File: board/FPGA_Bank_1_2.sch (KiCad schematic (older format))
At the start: 3 parts, among them SW1 SW_PUSH, U10 XC6SLX150T

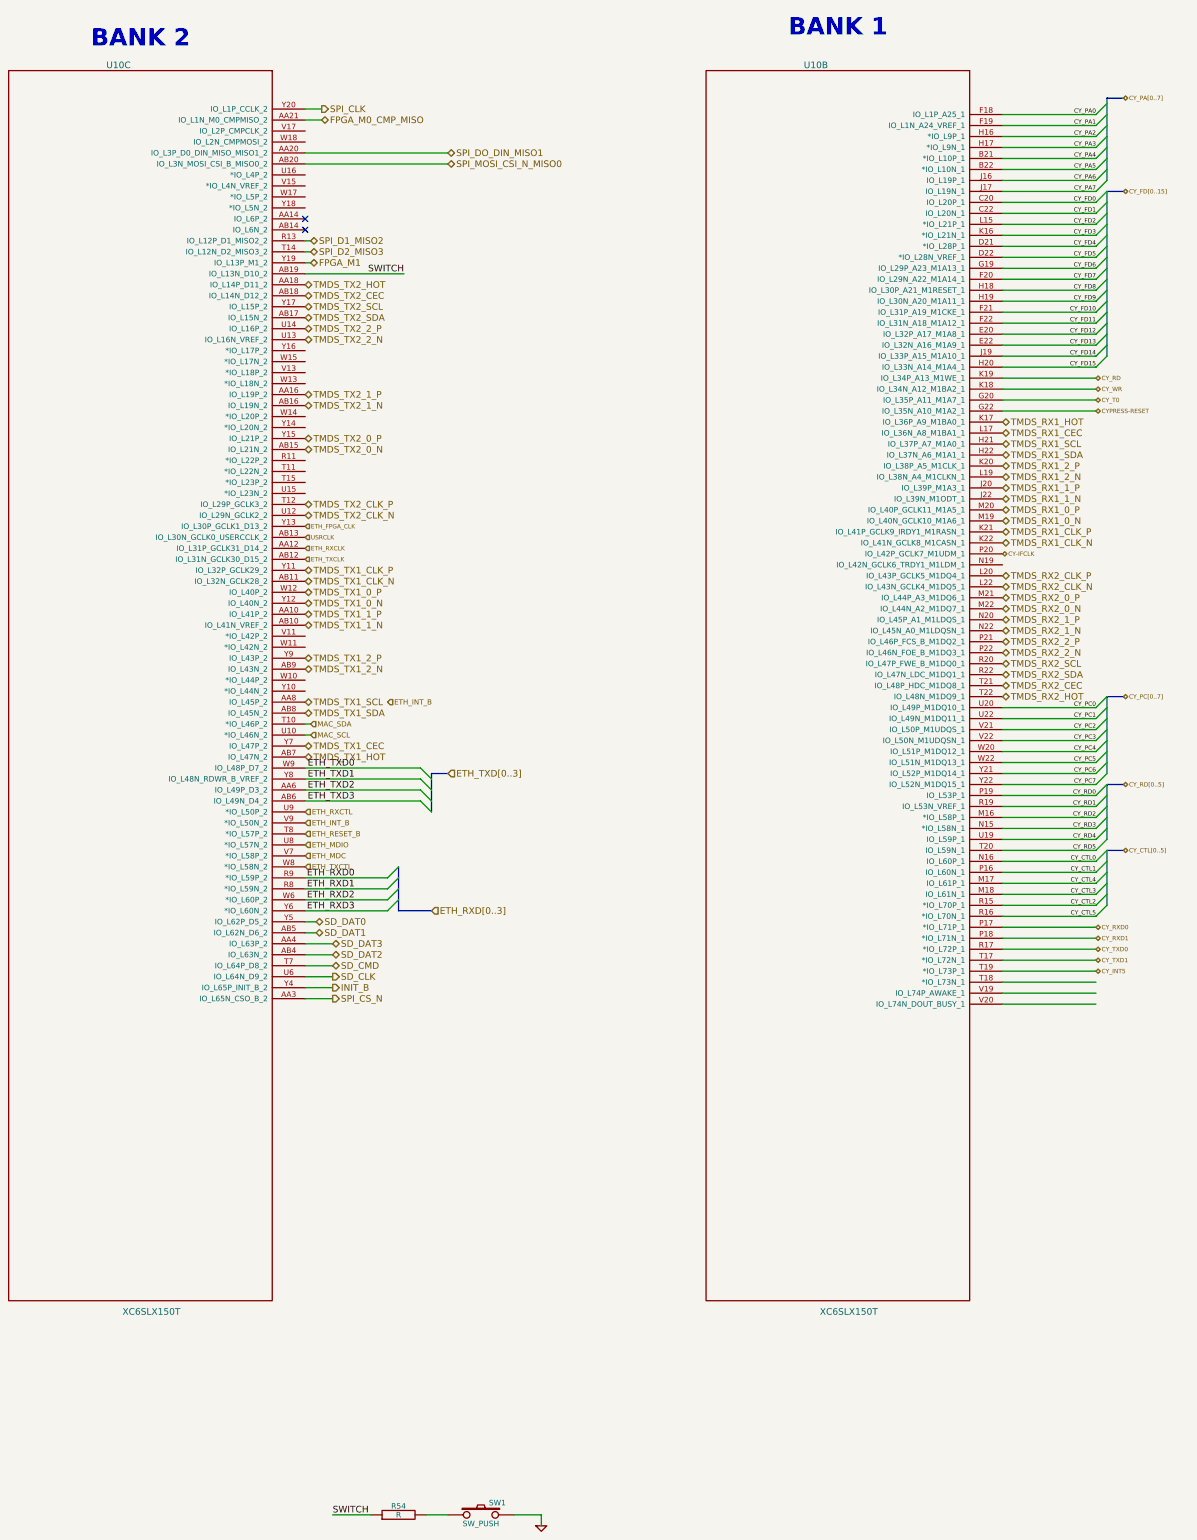
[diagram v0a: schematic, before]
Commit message: Issue #1680 - Bank 0 Ios
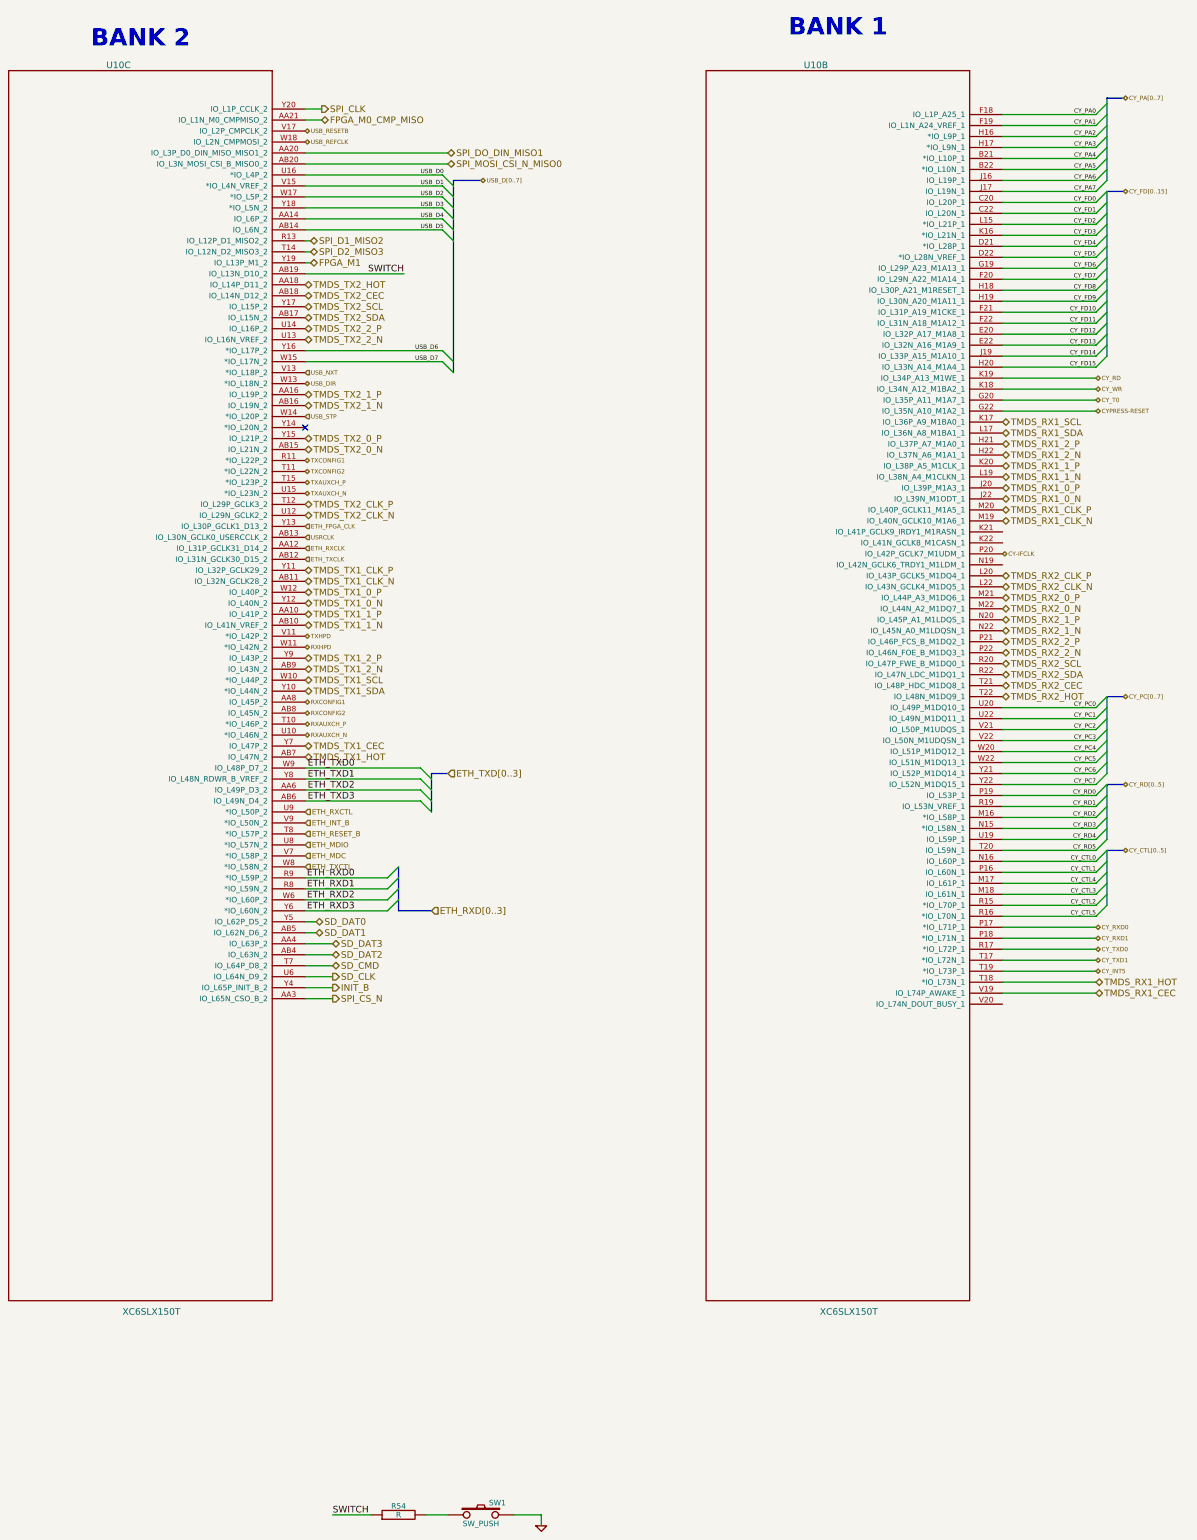
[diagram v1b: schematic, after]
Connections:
- net TMDS_RX1_0_N: now also U10.J22 (IO_L39N_M1ODT_1); no longer U10.M19 (IO_L40N_GCLK10_M1A6_1)
- net TMDS_RX1_0_P: now also U10.J20 (IO_L39P_M1A3_1); no longer U10.M20 (IO_L40P_GCLK11_M1A5_1)
- net TMDS_RX1_1_N: now also U10.L19 (IO_L38N_A4_M1CLKN_1); no longer U10.J22 (IO_L39N_M1ODT_1)
- net TMDS_RX1_1_P: now also U10.K20 (IO_L38P_A5_M1CLK_1); no longer U10.J20 (IO_L39P_M1A3_1)
- net TMDS_RX1_2_N: now also U10.H22 (IO_L37N_A6_M1A1_1); no longer U10.L19 (IO_L38N_A4_M1CLKN_1)
- net TMDS_RX1_2_P: now also U10.H21 (IO_L37P_A7_M1A0_1); no longer U10.K20 (IO_L38P_A5_M1CLK_1)
- net TMDS_RX1_CEC: now also U10.V19 (IO_L74P_AWAKE_1); no longer U10.L17 (IO_L36N_A8_M1BA1_1)
- net TMDS_RX1_CLK_N: now also U10.M19 (IO_L40N_GCLK10_M1A6_1); no longer U10.K22 (IO_L41N_GCLK8_M1CASN_1)
- net TMDS_RX1_CLK_P: now also U10.M20 (IO_L40P_GCLK11_M1A5_1); no longer U10.K21 (IO_L41P_GCLK9_IRDY1_M1RASN_1)
- net TMDS_RX1_HOT: now also U10.T18 (*IO_L73N_1); no longer U10.K17 (IO_L36P_A9_M1BA0_1)
- net TMDS_RX1_SCL: now also U10.K17 (IO_L36P_A9_M1BA0_1); no longer U10.H21 (IO_L37P_A7_M1A0_1)
- net TMDS_RX1_SDA: now also U10.L17 (IO_L36N_A8_M1BA1_1); no longer U10.H22 (IO_L37N_A6_M1A1_1)
- net TMDS_TX1_SCL: now also U10.W10 (*IO_L44P_2); no longer U10.AA8 (IO_L45P_2)
- net TMDS_TX1_SDA: now also U10.Y10 (*IO_L44N_2); no longer U10.AB8 (IO_L45N_2)
- net USB_D4: now reaches U10.AA14 (IO_L6P_2)
- net USB_D5: now reaches U10.AB14 (IO_L6N_2)
- net TXCONFIG1: now reaches U10.R11 (*IO_L22P_2)
- net TXCONFIG2: now reaches U10.T11 (*IO_L22N_2)
- net TXAUXCH_P: now reaches U10.T15 (*IO_L23P_2)
- net TXAUXCH_N: now reaches U10.U15 (*IO_L23N_2)
- net USB_D0: now reaches U10.U16 (*IO_L4P_2)
- net TXHPD: now reaches U10.V11 (*IO_L42P_2)
- net USB_NXT: now reaches U10.V13 (*IO_L18P_2)
- net USB_D1: now reaches U10.V15 (*IO_L4N_VREF_2)
- net USB_RESETB: now reaches U10.V17 (IO_L2P_CMPCLK_2)
- net RXHPD: now reaches U10.W11 (*IO_L42N_2)
- net USB_DIR: now reaches U10.W13 (*IO_L18N_2)
- net USB_STP: now reaches U10.W14 (*IO_L20P_2)
- net USB_D7: now reaches U10.W15 (*IO_L17N_2)
- net USB_D2: now reaches U10.W17 (*IO_L5P_2)
- net USB_REFCLK: now reaches U10.W18 (IO_L2N_CMPMOSI_2)
- net USB_D6: now reaches U10.Y16 (*IO_L17P_2)
- net USB_D3: now reaches U10.Y18 (*IO_L5N_2)
- net MAC_SCL renamed RXAUXCH_N
- net MAC_SDA renamed RXAUXCH_P
- new net RXCONFIG1: U10.AA8 (IO_L45P_2)
- new net RXCONFIG2: U10.AB8 (IO_L45N_2)
- no-connect marks 2 -> 1
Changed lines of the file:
@@
 $Descr A2 23386 16535
 encoding utf-8
-Sheet 12 12
+Sheet 9 12
 Title "HDMI2USB"
-Date "12 mar 2015"
+Date "23 mar 2015"
 Rev "Rev2"
 Comp ""
@@
 	8250 14500 8250 14600
 $Comp
-L GND #PWR047
+L GND #PWR039
 U 1 1 53857D31
 P 8250 14600
-F 0 "#PWR047" H 8250 14600 30  0001 C CNN
+F 0 "#PWR039" H 8250 14600 30  0001 C CNN
 F 1 "GND" H 8250 14530 30  0001 C CNN
 F 2 "" H 8250 14600 60  0000 C CNN
@@
 	1    0    0    -1
 $EndComp
-NoConn ~ 6100 2700
-NoConn ~ 6100 2800
 Wire Wire Line
 	6100 3200 7000 3200
@@
 Text HLabel 6100 6000 2    60   BiDi ~ 0
 TMDS_TX1_CLK_N
-Text HLabel 6100 7100 2    60   BiDi ~ 0
+Text HLabel 6100 6900 2    60   BiDi ~ 0
 TMDS_TX1_SCL
-Text HLabel 6100 7200 2    60   BiDi ~ 0
+Text HLabel 6100 7000 2    60   BiDi ~ 0
 TMDS_TX1_SDA
 Text HLabel 6100 7500 2    60   BiDi ~ 0
@@
 Text HLabel 6100 3300 2    60   BiDi ~ 0
 TMDS_TX2_HOT
+Text HLabel 12450 5150 2    60   BiDi ~ 0
+TMDS_RX1_0_P
+Text HLabel 12450 5250 2    60   BiDi ~ 0
+TMDS_RX1_0_N
+Text HLabel 12450 4950 2    60   BiDi ~ 0
+TMDS_RX1_1_P
+Text HLabel 12450 5050 2    60   BiDi ~ 0
+TMDS_RX1_1_N
+Text HLabel 12450 4750 2    60   BiDi ~ 0
+TMDS_RX1_2_P
+Text HLabel 12450 4850 2    60   BiDi ~ 0
+TMDS_RX1_2_N
 Text HLabel 12450 5350 2    60   BiDi ~ 0
-TMDS_RX1_0_P
+TMDS_RX1_CLK_P
 Text HLabel 12450 5450 2    60   BiDi ~ 0
-TMDS_RX1_0_N
-Text HLabel 12450 5150 2    60   BiDi ~ 0
-TMDS_RX1_1_P
-Text HLabel 12450 5250 2    60   BiDi ~ 0
-TMDS_RX1_1_N
-Text HLabel 12450 4950 2    60   BiDi ~ 0
-TMDS_RX1_2_P
-Text HLabel 12450 5050 2    60   BiDi ~ 0
-TMDS_RX1_2_N
-Text HLabel 12450 5550 2    60   BiDi ~ 0
-TMDS_RX1_CLK_P
-Text HLabel 12450 5650 2    60   BiDi ~ 0
 TMDS_RX1_CLK_N
-Text HLabel 12450 4750 2    60   BiDi ~ 0
+Text HLabel 12450 4550 2    60   BiDi ~ 0
 TMDS_RX1_SCL
-Text HLabel 12450 4850 2    60   BiDi ~ 0
+Text HLabel 12450 4650 2    60   BiDi ~ 0
 TMDS_RX1_SDA
-Text HLabel 12450 4650 2    60   BiDi ~ 0
+Text HLabel 13300 9750 2    60   BiDi ~ 0
 TMDS_RX1_CEC
-Text HLabel 12450 4550 2    60   BiDi ~ 0
+Text HLabel 13300 9650 2    60   BiDi ~ 0
 TMDS_RX1_HOT
 Text HLabel 12450 6150 2    60   BiDi ~ 0
@@
 Text HLabel 7400 7750 2    60   Input ~ 0
 ETH_TXD[0..3]
-Text HLabel 6150 7400 2    47   Input ~ 0
-MAC_SCL
-Text HLabel 6150 7300 2    47   Input ~ 0
-MAC_SDA
-Wire Wire Line
-	6150 7300 6100 7300
-Wire Wire Line
-	6100 7400 6150 7400
 Wire Wire Line
 	6100 8000 7150 8000
@@
 Wire Wire Line
 	6100 7700 7150 7700
-Text HLabel 6850 7100 2    47   Input ~ 0
-ETH_INT_B
 Text HLabel 6100 5500 2    39   Input ~ 0
 ETH_FPGA_CLK
@@
 Wire Wire Line
 	12450 9750 13300 9750
-Wire Wire Line
-	12450 9850 13300 9850
 Entry Wire Line
 	13300 1750 13400 1650
@@
 Text Notes 10500 1050 0    157  ~ 31
 BANK 1
+Text HLabel 6100 2000 2    39   BiDi ~ 0
+USB_REFCLK
+Text HLabel 6100 4100 2    39   Input ~ 0
+USB_NXT
+Text HLabel 6100 4200 2    39   BiDi ~ 0
+USB_DIR
+Text HLabel 6100 4500 2    39   Input ~ 0
+USB_STP
+Text HLabel 6100 1900 2    39   BiDi ~ 0
+USB_RESETB
+Text HLabel 7700 2350 2    39   BiDi ~ 0
+USB_D[0..7]
+Text Label 7150 2300 0    39   ~ 0
+USB_D0
+Text Label 7150 2400 0    39   ~ 0
+USB_D1
+Text Label 7150 2500 0    39   ~ 0
+USB_D2
+Text Label 7150 2600 0    39   ~ 0
+USB_D3
+Text Label 7150 2700 0    39   ~ 0
+USB_D4
+Text Label 7150 2800 0    39   ~ 0
+USB_D5
+Text Label 7100 3900 0    39   ~ 0
+USB_D6
+Text Label 7100 4000 0    39   ~ 0
+USB_D7
+Wire Wire Line
+	6100 3900 7350 3900
+Wire Wire Line
+	6100 4000 7350 4000
+Wire Wire Line
+	6100 2300 7350 2300
+Wire Wire Line
+	6100 2400 7350 2400
+Wire Wire Line
+	6100 2500 7350 2500
+Wire Wire Line
+	6100 2600 7350 2600
+Wire Wire Line
+	6100 2700 7350 2700
+Wire Wire Line
+	6100 2800 7350 2800
+Entry Wire Line
+	7350 4000 7450 4100
+Entry Wire Line
+	7350 3900 7450 4000
+Entry Wire Line
+	7350 2800 7450 2900
+Entry Wire Line
+	7350 2700 7450 2800
+Entry Wire Line
+	7350 2600 7450 2700
+Entry Wire Line
+	7350 2500 7450 2600
+Entry Wire Line
+	7350 2400 7450 2500
+Entry Wire Line
+	7350 2300 7450 2400
+Wire Bus Line
+	7450 4100 7450 2350
+Wire Bus Line
+	7450 2350 7700 2350
+NoConn ~ 6100 4600
+Text HLabel 6100 4900 2    39   BiDi ~ 0
+TXCONFIG1
+Text HLabel 6100 5000 2    39   BiDi ~ 0
+TXCONFIG2
+Text HLabel 6100 5200 2    39   BiDi ~ 0
+TXAUXCH_N
+Text HLabel 6100 5100 2    39   BiDi ~ 0
+TXAUXCH_P
+Text HLabel 6100 6500 2    39   BiDi ~ 0
+TXHPD
+Text HLabel 6100 6600 2    39   BiDi ~ 0
+RXHPD
+Text HLabel 6100 7100 2    39   BiDi ~ 0
+RXCONFIG1
+Text HLabel 6100 7200 2    39   BiDi ~ 0
+RXCONFIG2
+Text HLabel 6100 7400 2    39   BiDi ~ 0
+RXAUXCH_N
+Text HLabel 6100 7300 2    39   BiDi ~ 0
+RXAUXCH_P
 $EndSCHEMATC

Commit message: Issue #1683
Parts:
- U10: value XC6SLX150T -> XC6SLX45T
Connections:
- net ETH_FPGA_CLK is gone; now on net USB_REFCLK: U10.Y13 (IO_L30P_GCLK1_D13_2)
- net USB_REFCLK: no longer U10.W18 (IO_L2N_CMPMOSI_2)
- net USB_STP: now also U10.W18 (IO_L2N_CMPMOSI_2); no longer U10.W14 (*IO_L20P_2)
- net RXAUXCH_N renamed DPRXAUXCH_N
- net RXAUXCH_P renamed DPRXAUXCH_P
- net RXCONFIG1 renamed DPRXCONFIG1
- net RXCONFIG2 renamed DPRXCONFIG2
- net RXHPD renamed DPRXHPD
- net TXAUXCH_N renamed DPTXAUXCH_N
- net TXAUXCH_P renamed DPTXAUXCH_P
- net TXCONFIG1 renamed DPTXCONFIG1
- net TXCONFIG2 renamed DPTXCONFIG2
- net TXHPD renamed DPTXHPD
- no-connect marks 1 -> 0
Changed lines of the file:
@@
 $Descr A2 23386 16535
 encoding utf-8
-Sheet 9 12
+Sheet 12 12
 Title "HDMI2USB"
-Date "23 mar 2015"
+Date "25 mar 2015"
 Rev "Rev2"
 Comp ""
@@
 P 5350 5350
 F 0 "U10" H 4400 9400 60  0000 C CNN
-F 1 "XC6SLX150T" H 4700 -1950 60  0000 C CNN
+F 1 "XC6SLX45T" H 4700 -1950 60  0000 C CNN
 F 2 "~" H 5400 5350 60  0000 C CNN
 F 3 "~" H 5400 5350 60  0000 C CNN
@@
 P 11700 5350
 F 0 "U10" H 10750 9400 60  0000 C CNN
-F 1 "XC6SLX150T" H 11050 -1950 60  0000 C CNN
+F 1 "XC6SLX45T" H 11050 -1950 60  0000 C CNN
 F 2 "~" H 11750 5350 60  0000 C CNN
 F 3 "~" H 11750 5350 60  0000 C CNN
@@
 	8250 14500 8250 14600
 $Comp
-L GND #PWR039
+L GND #PWR043
 U 1 1 53857D31
 P 8250 14600
-F 0 "#PWR039" H 8250 14600 30  0001 C CNN
+F 0 "#PWR043" H 8250 14600 30  0001 C CNN
 F 1 "GND" H 8250 14530 30  0001 C CNN
 F 2 "" H 8250 14600 60  0000 C CNN
@@
 Wire Wire Line
 	6100 7700 7150 7700
-Text HLabel 6100 5500 2    39   Input ~ 0
-ETH_FPGA_CLK
 Text HLabel 6100 5700 2    39   Input ~ 0
 ETH_RXCLK
@@
 Text Notes 10500 1050 0    157  ~ 31
 BANK 1
-Text HLabel 6100 2000 2    39   BiDi ~ 0
+Text HLabel 6100 5500 2    39   BiDi ~ 0
 USB_REFCLK
 Text HLabel 6100 4100 2    39   Input ~ 0
@@
 Text HLabel 6100 4200 2    39   BiDi ~ 0
 USB_DIR
-Text HLabel 6100 4500 2    39   Input ~ 0
+Text HLabel 6100 2000 2    39   Input ~ 0
 USB_STP
 Text HLabel 6100 1900 2    39   BiDi ~ 0
@@
 Wire Bus Line
 	7450 2350 7700 2350
-NoConn ~ 6100 4600
 Text HLabel 6100 4900 2    39   BiDi ~ 0
-TXCONFIG1
+DPTXCONFIG1
 Text HLabel 6100 5000 2    39   BiDi ~ 0
-TXCONFIG2
+DPTXCONFIG2
 Text HLabel 6100 5200 2    39   BiDi ~ 0
-TXAUXCH_N
+DPTXAUXCH_N
 Text HLabel 6100 5100 2    39   BiDi ~ 0
-TXAUXCH_P
+DPTXAUXCH_P
 Text HLabel 6100 6500 2    39   BiDi ~ 0
-TXHPD
+DPTXHPD
 Text HLabel 6100 6600 2    39   BiDi ~ 0
-RXHPD
+DPRXHPD
 Text HLabel 6100 7100 2    39   BiDi ~ 0
-RXCONFIG1
+DPRXCONFIG1
 Text HLabel 6100 7200 2    39   BiDi ~ 0
-RXCONFIG2
+DPRXCONFIG2
 Text HLabel 6100 7400 2    39   BiDi ~ 0
-RXAUXCH_N
+DPRXAUXCH_N
 Text HLabel 6100 7300 2    39   BiDi ~ 0
-RXAUXCH_P
+DPRXAUXCH_P
 $EndSCHEMATC

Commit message: Issue #1670
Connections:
- no-connect marks 0 -> 6
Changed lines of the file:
@@
 $Descr A2 23386 16535
 encoding utf-8
-Sheet 12 12
+Sheet 11 12
 Title "HDMI2USB"
-Date "25 mar 2015"
+Date "30 mar 2015"
 Rev "Rev2"
 Comp ""
@@
 Text HLabel 6100 7300 2    39   BiDi ~ 0
 DPRXAUXCH_P
+NoConn ~ 6100 4500
+NoConn ~ 6100 4600
+NoConn ~ 12450 5850
+NoConn ~ 12450 5650
+NoConn ~ 12450 5550
+NoConn ~ 12450 9850
 $EndSCHEMATC

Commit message: Issue #1585
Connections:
- net SMCLK: now reaches U10.W14 (*IO_L20P_2)
- net SMDATA: now reaches U10.Y14 (*IO_L20N_2)
- net MGTREFCLK0_101_P: now reaches U10.K21 (IO_L41P_GCLK9_IRDY1_M1RASN_1)
- net MGTREFCLK0_101_N: now reaches U10.K22 (IO_L41N_GCLK8_M1CASN_1)
- net 27Mhz: now reaches U10.N19 (IO_L42N_GCLK6_TRDY1_M1LDM_1)
- no-connect marks 6 -> 1
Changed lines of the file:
@@
 LIBS:contrib
 LIBS:valves
-LIBS:hdmi2usb
-LIBS:timvideos-pcie-8x
 LIBS:HDMI2USB-cache
 EELAYER 27 0
@@
 Sheet 11 12
 Title "HDMI2USB"
-Date "30 mar 2015"
+Date "1 apr 2015"
 Rev "Rev2"
 Comp ""
@@
 	8250 14500 8250 14600
 $Comp
-L GND #PWR43
+L GND #PWR052
 U 1 1 53857D31
 P 8250 14600
-F 0 "#PWR43" H 8250 14600 30  0001 C CNN
+F 0 "#PWR052" H 8250 14600 30  0001 C CNN
 F 1 "GND" H 8250 14530 30  0001 C CNN
 F 2 "" H 8250 14600 60  0000 C CNN
@@
 Text HLabel 6100 7300 2    39   BiDi ~ 0
 DPRXAUXCH_P
-NoConn ~ 6100 4500
-NoConn ~ 6100 4600
-NoConn ~ 12450 5850
-NoConn ~ 12450 5650
-NoConn ~ 12450 5550
 NoConn ~ 12450 9850
+Text HLabel 12450 5850 2    39   Input ~ 0
+27Mhz
+Text HLabel 12450 5550 2    39   BiDi ~ 0
+MGTREFCLK0_101_P
+Text HLabel 12450 5650 2    39   BiDi ~ 0
+MGTREFCLK0_101_N
+Text HLabel 6100 4500 2    39   BiDi ~ 0
+SMCLK
+Text HLabel 6100 4600 2    39   BiDi ~ 0
+SMDATA
 $EndSCHEMATC
